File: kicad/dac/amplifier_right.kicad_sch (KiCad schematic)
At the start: 29 parts, among them Q2 PNP, Q3 PNP, Q4 NPN, Q5 NPN, Q6 NPN, Q7 PNP, Q8 NPN, Q9 PNP

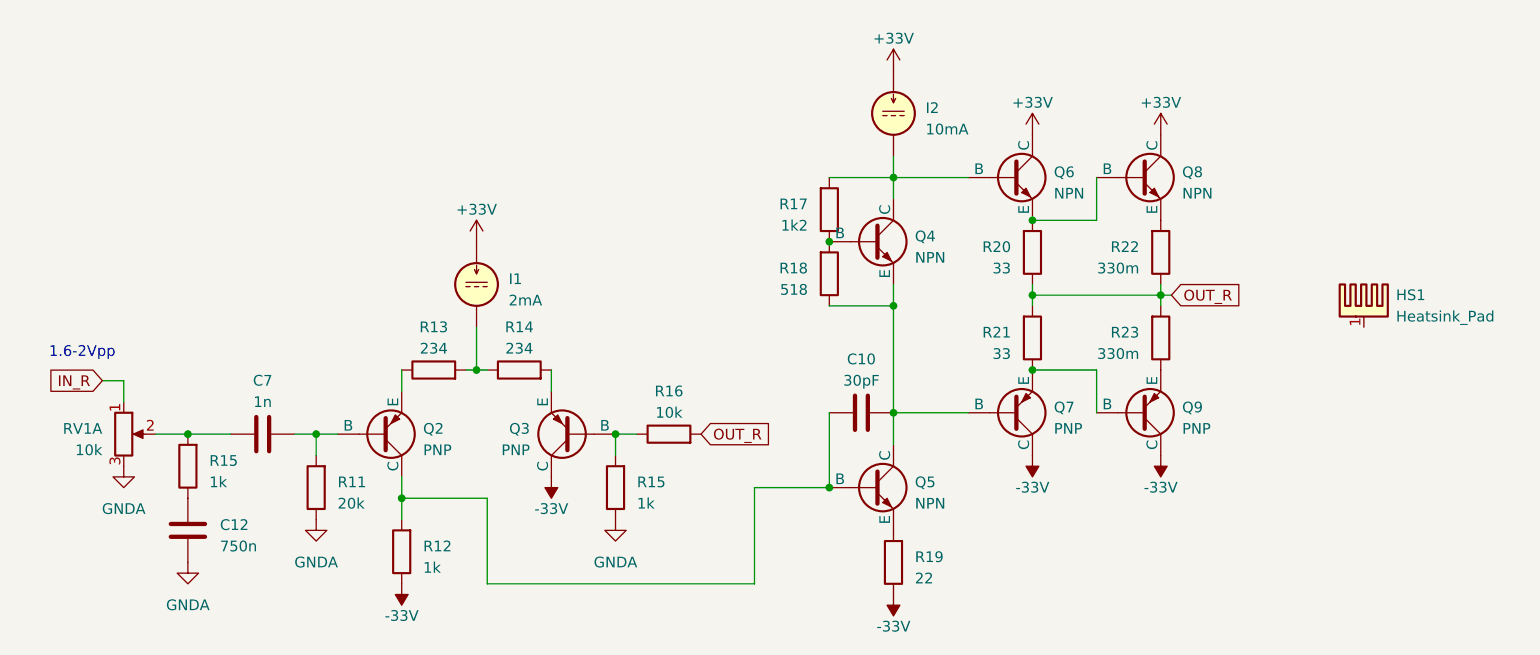
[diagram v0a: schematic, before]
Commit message: split power supply to different board
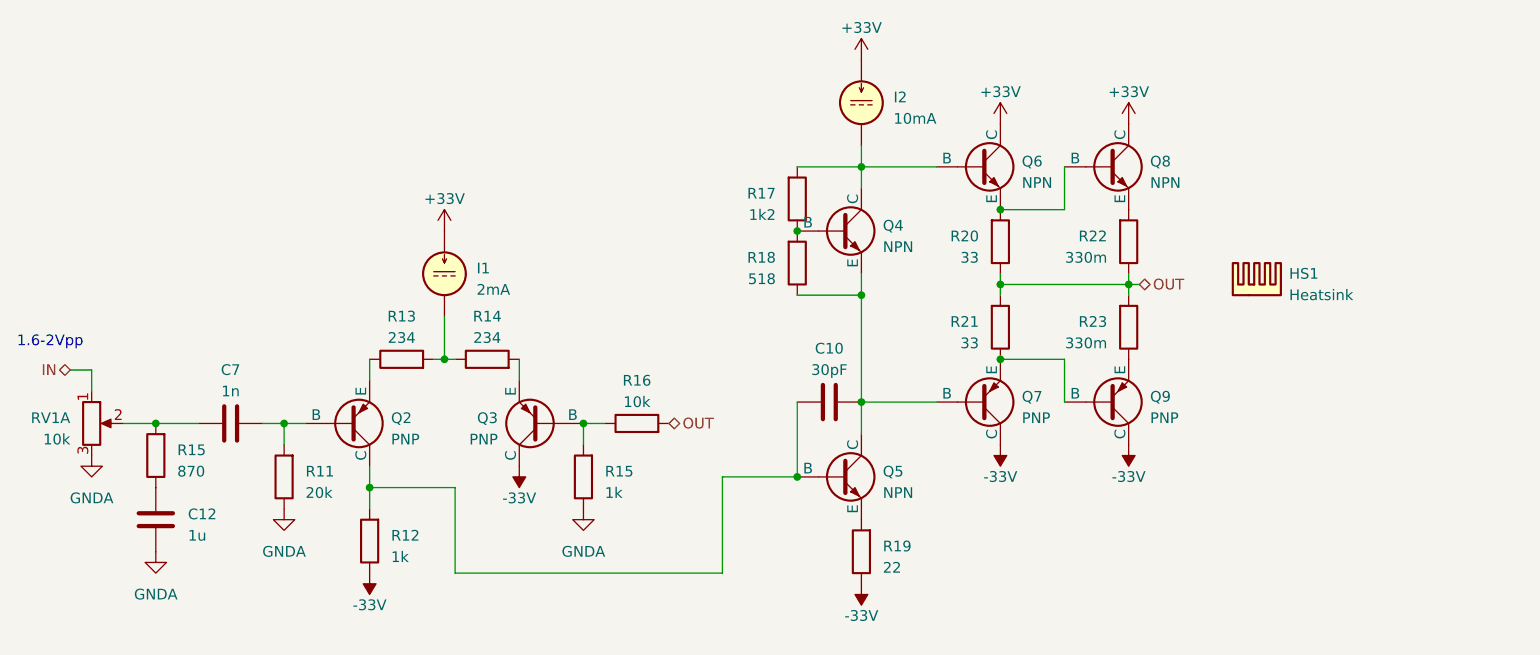
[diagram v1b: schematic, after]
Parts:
- removed HS1: Heatsink_Pad, symbol Mechanical:Heatsink_Pad
- removed R15 (x2): 1k, Resistor_THT:R_Axial_DIN0207_L6.3mm_D2.5mm_P10.16mm_Horizontal, symbol Device:R
- added HS1: Heatsink, Heatsink:Heatsink_Fischer_SK104-STCB_35x13mm__2xDrill3.5mm_ScrewM3, symbol Mechanical:Heatsink
- added R15: 1k, Resistor_THT:R_Axial_DIN0207_L6.3mm_D2.5mm_P10.16mm_Horizontal, symbol Device:R
- added R15: 870, Resistor_THT:R_Axial_DIN0207_L6.3mm_D2.5mm_P10.16mm_Horizontal, symbol Device:R
- C12: value 750n -> 1u
- Q4: footprint (none) -> Package_TO_SOT_THT:TO-92L_Inline
- Q8, Q9: footprint (none) -> Package_TO_SOT_THT:TO-220-3_Vertical
- RV1: footprint (none) -> library:RK09L12B
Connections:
- net GNDA: now also R15.1
- net at Q3.2 (B), R16.1: now also R15.2
- net at C7.1, RV1.2: now also R15.2
- net at C12.1: now also R15.1
- net IN_R renamed IN
- net OUT_R renamed OUT

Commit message: Commit
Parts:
- removed C12: 1u, symbol Device:C
- removed I1: 2mA, symbol Simulation_SPICE:IDC
- removed I2: 10mA, symbol Simulation_SPICE:IDC
- removed Q2, Q3: PNP, symbol Simulation_SPICE:PNP
- removed Q4: NPN, Package_TO_SOT_THT:TO-92L_Inline, symbol Simulation_SPICE:NPN
- removed Q5: NPN, symbol Simulation_SPICE:NPN
- removed R12, R15: 1k, Resistor_THT:R_Axial_DIN0207_L6.3mm_D2.5mm_P10.16mm_Horizontal, symbol Device:R
- removed R13: 234, Resistor_THT:R_Axial_DIN0207_L6.3mm_D2.5mm_P10.16mm_Horizontal, symbol Device:R
- removed R15: 870, Resistor_THT:R_Axial_DIN0207_L6.3mm_D2.5mm_P10.16mm_Horizontal, symbol Device:R
- removed R19: 22, Resistor_THT:R_Axial_DIN0207_L6.3mm_D2.5mm_P10.16mm_Horizontal, symbol Device:R
- removed R20, R21: 33, Resistor_THT:R_Axial_DIN0207_L6.3mm_D2.5mm_P10.16mm_Horizontal, symbol Device:R
- removed R22, R23: 330m, symbol Device:R
- added C11: 120p, symbol Device:C
- added C19: 10u, Capacitor_THT:CP_Radial_D5.0mm_P2.50mm, symbol Device:C_Polarized
- added C20, C21: 10u, symbol Device:C
- added C22, C23: 100u, symbol Device:C_Polarized
- added Q10, Q6: PNP, Package_SO:SC-74-6_1.5x2.9mm_P0.95mm, symbol library:Dual-PNP
- added Q4 (x3): NPN, Package_TO_SOT_THT:TO-92, symbol Simulation_SPICE:NPN
- added unit 2 of Q6
- added unit 2 of Q7
- added Q8: NPN, Package_SO:SC-74-6_1.5x2.9mm_P0.95mm, symbol library:Dual-NPN
- added unit 2 of Q8
- added R12 (x2): 470, Resistor_SMD:R_1206_3216Metric_Pad1.30x1.75mm_HandSolder, symbol Device:R
- added R13: 68, Resistor_THT:R_Axial_DIN0207_L6.3mm_D2.5mm_P10.16mm_Horizontal, symbol Device:R
- added R13: 430, Resistor_SMD:R_1206_3216Metric_Pad1.30x1.75mm_HandSolder, symbol Device:R
- added R13 (x2), R15: 68, Resistor_SMD:R_1206_3216Metric_Pad1.30x1.75mm_HandSolder, symbol Device:R
- added R15 (x2): 27k, Resistor_SMD:R_1206_3216Metric_Pad1.30x1.75mm_HandSolder, symbol Device:R
- added R15: 2k, Resistor_THT:R_Axial_DIN0207_L6.3mm_D2.5mm_P10.16mm_Horizontal, symbol Device:R
- added R15: 680, Resistor_SMD:R_1206_3216Metric_Pad1.30x1.75mm_HandSolder, symbol Device:R
- added R19: 2k2, Resistor_SMD:R_1206_3216Metric_Pad1.30x1.75mm_HandSolder, symbol Device:R
- added R19: 22, Resistor_SMD:R_1206_3216Metric_Pad1.30x1.75mm_HandSolder, symbol Device:R
- added R20 (x2): 33, Resistor_SMD:R_1206_3216Metric_Pad1.30x1.75mm_HandSolder, symbol Device:R
- added R35: 500, symbol Device:R_Trim
- added R37: 100, Resistor_SMD:R_1206_3216Metric_Pad1.30x1.75mm_HandSolder, symbol Device:R
- added R9 (x2): 1, Resistor_THT:R_Axial_DIN0614_L14.3mm_D5.7mm_P20.32mm_Horizontal, symbol Device:R
- added RV2: 100, symbol Device:R_Potentiometer_Trim
- C10: footprint (none) -> Capacitor_SMD:C_1206_3216Metric_Pad1.33x1.80mm_HandSolder
- C7: value 1n -> 2u2
- HS1: footprint Heatsink:Heatsink_Fischer_SK104-STCB_35x13mm__2xDrill3.5mm_ScrewM3 -> Heatsink:Heatsink_Fischer_SK129-STS_42x25mm_2xDrill2.5mm; Digikey (none) -> HS404-ND; DigikeyAlt (none) -> FA-T220-25E-ND; Height (none) -> 25.4mm
- R14: value 234 -> 430; footprint Resistor_THT:R_Axial_DIN0207_L6.3mm_D2.5mm_P10.16mm_Horizontal -> Resistor_SMD:R_1206_3216Metric_Pad1.30x1.75mm_HandSolder
- R16: value 10k -> 20k
- R17: value 1k2 -> 2k2; footprint Resistor_THT:R_Axial_DIN0207_L6.3mm_D2.5mm_P10.16mm_Horizontal -> Resistor_SMD:R_1206_3216Metric_Pad1.30x1.75mm_HandSolder
- R18: value 518 -> 680; footprint Resistor_THT:R_Axial_DIN0207_L6.3mm_D2.5mm_P10.16mm_Horizontal -> Resistor_SMD:R_1206_3216Metric_Pad1.30x1.75mm_HandSolder
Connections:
- net GNDA: now also C11.2, C20.2, C21.1, C22.2, C23.1, Q4.1 (C), R15.1, R15.1, R15.1
- net IN: now also R13.1; no longer RV1.1
- net OUT: now also R20.1, R20.2, R9.1, R9.2
- net at R16.1: now also Q6.2 (B), R15.2
- net at R14.1: now also R13.1, RV2.3
- net at R14.2: now also Q6.4 (E)
- net at C10.2, Q7.2 (B): now also C19.2, Q4.1 (C), Q4.3 (E), R35.2; no longer R18.1
- net at Q7.3 (E), Q9.2 (B): now also R20.1
- net at Q6.2 (B): now also C19.1, Q4.1 (C), R37.2; no longer R17.2
- net at R17.1, R18.2: now also Q4.2 (B)
- net at Q8.3 (E): now also R9.1
- net at Q9.3 (E): now also R9.2
- net at Q6.3 (E), Q8.2 (B): now also R20.2
- net at C7.2, R11.2: now also Q6.1 (B)
- net at C10.1: now also Q4.2 (B), Q6.6 (C), Q8.6 (C)
- net +36V renamed +30V
- net +30V: now also C20.1, C22.1, Q10.5 (E), Q7.5 (E), R15.2, R15.2
- net -36V renamed -30V
- net -30V: now also C21.2, C23.2, R12.1, R12.1, R19.1, R19.1
- new net: Q8.5 (E), R12.2
- new net: Q6.5 (E), R13.1
- new net: C11.1, R13.2, RV1.1
- new net: Q8.4 (E), R12.2
- new net: R13.1, R13.2, RV2.1
- new net: R18.1, R35.1
- new net: Q4.2 (B), Q4.3 (E), R19.2
- new net: Q7.2 (B), Q7.6 (C), R15.2
- new net: Q7.3 (C), R13.2, R13.2, RV2.2
- new net: Q7.1 (B), Q7.4 (E), R15.1
- new net: Q4.3 (E), R19.2
- new net: Q10.1 (B), Q10.4 (E), R15.1
- new net: Q6.3 (C), Q8.1 (B), Q8.2 (B), Q8.3 (C)
- new net: Q10.3 (C), R17.2, R37.1
- new net: Q10.2 (B), Q10.6 (C), R15.2
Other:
- note added: "0.5mA"
- note added: "1.7V above V-"
- note added: "10mA"
- note added: "1mA"
- note added: "=Vbe factor * re'"
- note added: "COPY"
- note added: "Iq=26mA"
- note added: "This sheet for the right channel amplifier is a copy from the left channel. Its design must NOT be changed. Beware of potentiometer A/B variants. All resistors are 1/4W 1206 unless specified."
- note added: "Vbias=4*Vbe"
- title: USB DAC & Headphone Amplifier -> Right Channel Amplifier
- moved on the sheet: RV1A

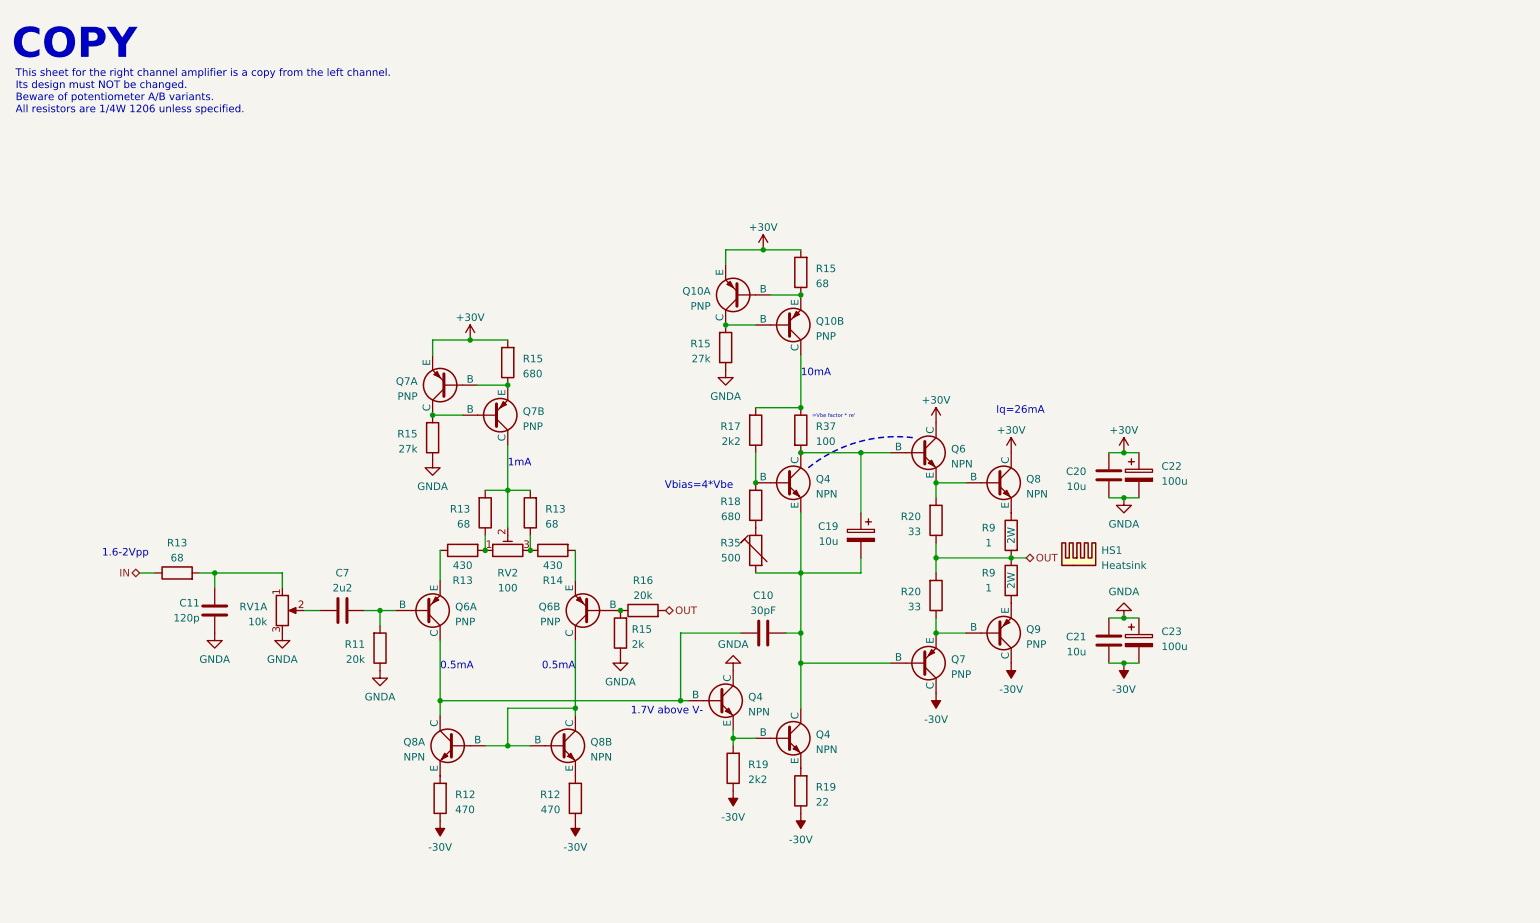
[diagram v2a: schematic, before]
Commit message: completed power supply footprints and placement
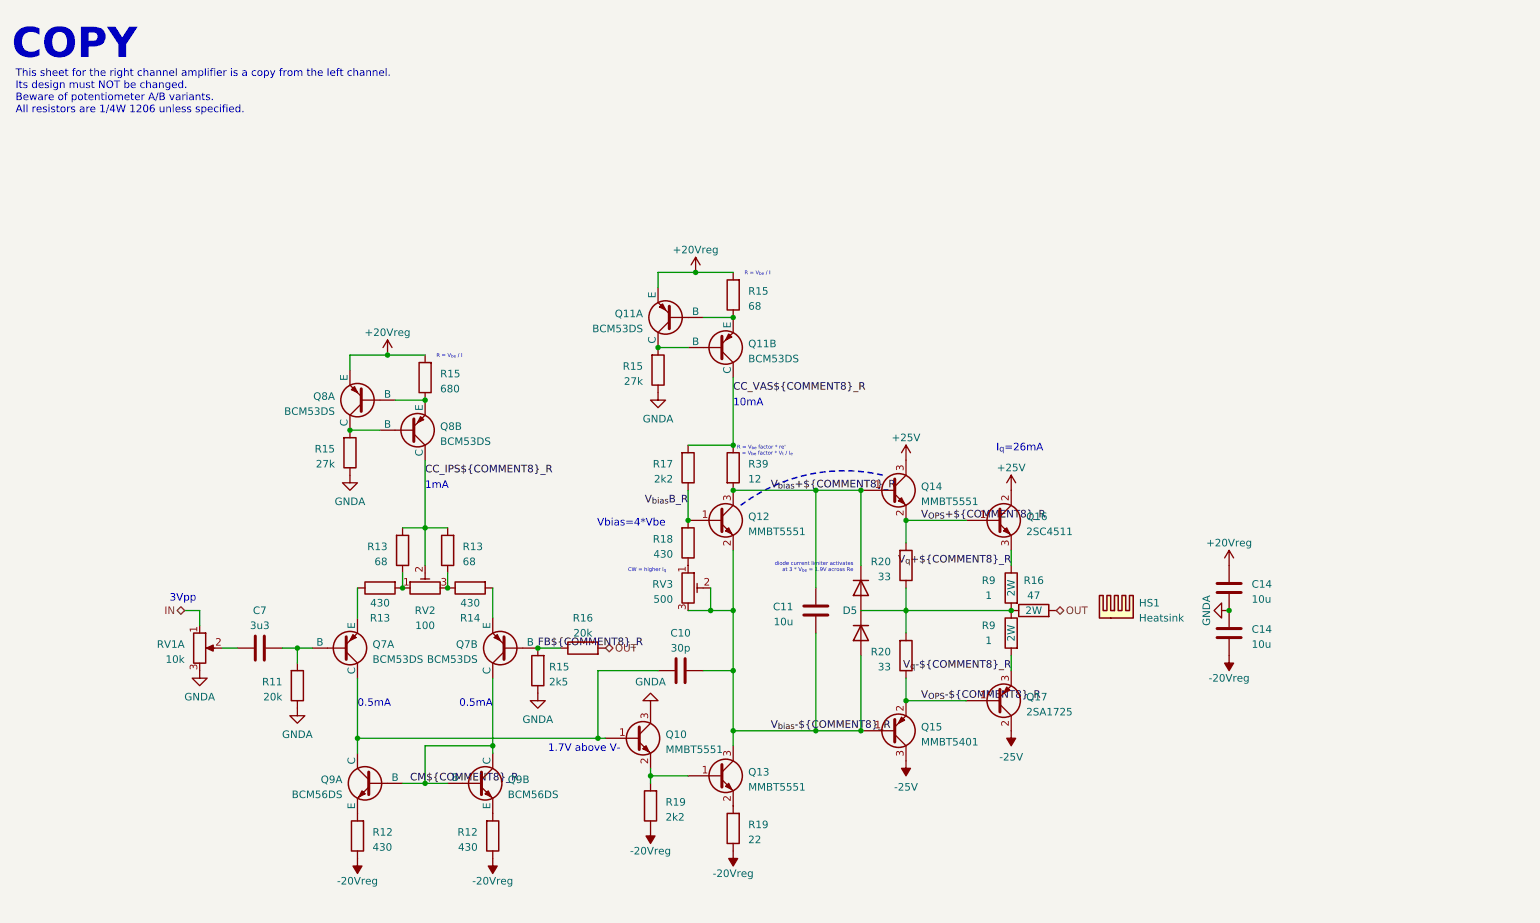
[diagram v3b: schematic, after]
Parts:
- removed C19: 10u, Capacitor_THT:CP_Radial_D5.0mm_P2.50mm, symbol Device:C_Polarized
- removed C20, C21: 10u, symbol Device:C
- removed C22, C23: 100u, symbol Device:C_Polarized
- removed Q10, Q6: PNP, Package_SO:SC-74-6_1.5x2.9mm_P0.95mm, symbol library:Dual-PNP
- removed Q4 (x3): NPN, Package_TO_SOT_THT:TO-92, symbol Simulation_SPICE:NPN
- removed Q6: NPN, symbol Simulation_SPICE:NPN
- removed Q7: PNP, symbol Simulation_SPICE:PNP
- removed Q8: NPN, Package_SO:SC-74-6_1.5x2.9mm_P0.95mm, symbol library:Dual-NPN
- removed Q8: NPN, Package_TO_SOT_THT:TO-220-3_Vertical, symbol Simulation_SPICE:NPN
- removed Q9: PNP, Package_TO_SOT_THT:TO-220-3_Vertical, symbol Simulation_SPICE:PNP
- removed R12 (x2): 470, Resistor_SMD:R_1206_3216Metric_Pad1.30x1.75mm_HandSolder, symbol Device:R
- removed R13: 68, Resistor_THT:R_Axial_DIN0207_L6.3mm_D2.5mm_P10.16mm_Horizontal, symbol Device:R
- removed R13: 430, Resistor_SMD:R_1206_3216Metric_Pad1.30x1.75mm_HandSolder, symbol Device:R
- removed R13 (x2), R15: 68, Resistor_SMD:R_1206_3216Metric_Pad1.30x1.75mm_HandSolder, symbol Device:R
- removed R15 (x2): 27k, Resistor_SMD:R_1206_3216Metric_Pad1.30x1.75mm_HandSolder, symbol Device:R
- removed R15: 2k, Resistor_THT:R_Axial_DIN0207_L6.3mm_D2.5mm_P10.16mm_Horizontal, symbol Device:R
- removed R15: 680, Resistor_SMD:R_1206_3216Metric_Pad1.30x1.75mm_HandSolder, symbol Device:R
- removed R16: 20k, Resistor_THT:R_Axial_DIN0207_L6.3mm_D2.5mm_P10.16mm_Horizontal, symbol Device:R
- removed R19: 2k2, Resistor_SMD:R_1206_3216Metric_Pad1.30x1.75mm_HandSolder, symbol Device:R
- removed R19: 22, Resistor_SMD:R_1206_3216Metric_Pad1.30x1.75mm_HandSolder, symbol Device:R
- removed R20 (x2): 33, Resistor_SMD:R_1206_3216Metric_Pad1.30x1.75mm_HandSolder, symbol Device:R
- removed R35: 500, symbol Device:R_Trim
- removed R37: 100, Resistor_SMD:R_1206_3216Metric_Pad1.30x1.75mm_HandSolder, symbol Device:R
- removed R9 (x2): 1, Resistor_THT:R_Axial_DIN0614_L14.3mm_D5.7mm_P20.32mm_Horizontal, symbol Device:R
- added C14 (x2): 10u, Capacitor_SMD:C_1206_3216Metric_Pad1.33x1.80mm_HandSolder, symbol Device:C
- added D5: ~, Package_TO_SOT_SMD:SOT-23-3, symbol library:Dual_Diode_Array
- added Q10, Q12, Q13, Q14: MMBT5551, Package_TO_SOT_SMD:SOT-23-3, symbol Device:Q_NPN_BEC
- added Q11, Q8: BCM53DS, Package_SO:SC-74-6_1.5x2.9mm_P0.95mm, symbol library:Dual-PNP
- added Q15: MMBT5401, Package_TO_SOT_SMD:SOT-23-3, symbol Device:Q_PNP_BEC
- added Q16: 2SC4511, Package_TO_SOT_THT:TO-220F-3_Vertical, symbol Device:Q_NPN_BCE
- added Q17: 2SA1725, Package_TO_SOT_THT:TO-220F-3_Vertical, symbol Device:Q_PNP_BCE
- added Q9: BCM56DS, Package_SO:SC-74-6_1.5x2.9mm_P0.95mm, symbol library:Dual-NPN
- added R12 (x2), R13: 430, Resistor_SMD:R_1206_3216Metric_Pad1.30x1.75mm_HandSolder, symbol Device:R
- added R13 (x2), R15: 68, Resistor_SMD:R_1206_3216Metric_Pad1.30x1.75mm_HandSolder, symbol Device:R
- added R15: 680, Resistor_SMD:R_1206_3216Metric_Pad1.30x1.75mm_HandSolder, symbol Device:R
- added R15 (x2): 27k, Resistor_SMD:R_1206_3216Metric_Pad1.30x1.75mm_HandSolder, symbol Device:R
- added R15: 2k5, Resistor_THT:R_Axial_DIN0207_L6.3mm_D2.5mm_P10.16mm_Horizontal, symbol Device:R
- added R16: 20k, Resistor_THT:R_Axial_DIN0207_L6.3mm_D2.5mm_P10.16mm_Horizontal, symbol Device:R
- added R16: 47, symbol Device:R
- added R19: 22, Resistor_SMD:R_1206_3216Metric_Pad1.30x1.75mm_HandSolder, symbol Device:R
- added R19: 2k2, Resistor_SMD:R_1206_3216Metric_Pad1.30x1.75mm_HandSolder, symbol Device:R
- added R20 (x2): 33, Resistor_SMD:R_1206_3216Metric_Pad1.30x1.75mm_HandSolder, symbol Device:R
- added R39: 12, Resistor_SMD:R_1206_3216Metric_Pad1.30x1.75mm_HandSolder, symbol Device:R
- added R9 (x2): 1, Resistor_THT:R_Axial_DIN0614_L14.3mm_D5.7mm_P20.32mm_Horizontal, symbol Device:R
- added RV3: 500, library:TC33, symbol Device:R_Potentiometer_Trim
- C10: value 30pF -> 30p
- C11: value 120p -> 10u; footprint (none) -> Capacitor_SMD:C_1206_3216Metric_Pad1.33x1.80mm_HandSolder; Digikey (none) -> 1276-3100-1-ND
- C7: value 2u2 -> 3u3; footprint (none) -> Capacitor_THT:C_Rect_L7.2mm_W7.2mm_P5.00mm_FKS2_FKP2_MKS2_MKP2; Digikey (none) -> 1928-1645-ND; Height (none) -> 13mm
- Q7: value PNP -> BCM53DS; footprint Package_SO:TSOP-6_1.65x3.05mm_P0.95mm -> Package_SO:SC-74-6_1.5x2.9mm_P0.95mm
- R18: value 680 -> 430
- RV2: footprint (none) -> library:TC33; Digikey (none) -> 118-TC33X-2-101GCT-ND
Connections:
- net GNDA: now also C14.1, C14.2, Q10.3 (C), R15.1, R15.1, R15.1; no longer C11.2
- net IN: now also RV1.1
- net OUT: now also R16.2, R16.2
- net at C7.2, R11.2: now also Q7.1 (B)
- net at C10.1: now also Q7.6 (C), Q10.1 (B), Q9.6 (C)
- net V_{bias}+${COMMENT8}${COMMENT9}: now reaches C11.1
- net V_{bias}+${COMMENT8}${COMMENT9}: now also D5.2 (C), Q12.3 (C), Q14.1 (B), R39.2; no longer RV1.1
- net V_{bias}-${COMMENT8}${COMMENT9}: now reaches C10.2
- net V_{bias}-${COMMENT8}${COMMENT9}: now also C11.2, D5.1 (A), Q12.2 (E), Q13.3 (C), Q15.1 (B), RV3.2, RV3.3
- net at RV2.1: now also R13.1, R13.2
- net at R18.1: now also RV3.1
- net FB${COMMENT8}${COMMENT9}: now reaches Q7.2 (B)
- net FB${COMMENT8}${COMMENT9}: now also R15.2, R16.1; no longer Q7.6 (C)
- net CC_IPS${COMMENT8}${COMMENT9}: now reaches RV2.2
- net CC_IPS${COMMENT8}${COMMENT9}: now also Q8.3 (C), R13.2, R13.2; no longer Q7.3 (C)
- net at Q7.4 (E): now also R14.2; no longer Q7.1 (B)
- net at R14.1, RV2.3: now also R13.1
- net CC_VAS${COMMENT8}${COMMENT9}: now reaches R17.2
- net CC_VAS${COMMENT8}${COMMENT9}: now also Q11.3 (C), R39.1
- net V_{bias}B${COMMENT9}: now reaches R17.1, R18.2
- net V_{bias}B${COMMENT9}: now also Q12.1 (B)
- net +30V: no longer names the net of Q7.5 (E)
- net +30V: now also R13.1
- new net: Q11.2 (B), Q11.6 (C), R15.2
- new net: Q11.1 (B), Q11.4 (E), R15.1
- new net: Q9.5 (E), R12.2
- new net: Q8.1 (B), Q8.4 (E), R15.1
- new net: Q8.2 (B), Q8.6 (C), R15.2
- new net: D5.3 (C/A), R16.1, R20.1, R20.2, R9.1, R9.2
- new net: Q10.2 (E), Q13.1 (B), R19.2
- new net: Q13.2 (E), R19.2
- new net: Q9.4 (E), R12.2
- new net +20Vreg: C14.1, Q11.5 (E), Q8.5 (E), R15.2, R15.2
- new net +25V: Q14.3 (C), Q16.2 (C)
- new net -20Vreg: C14.2, R12.1, R12.1, R19.1, R19.1
- new net -25V: Q15.3 (C), Q17.2 (C)
- new net CM${COMMENT8}${COMMENT9}: Q7.3 (C), Q9.1 (B), Q9.2 (B), Q9.3 (C)
- new net V_{OPS}+${COMMENT8}${COMMENT9}: Q14.2 (E), Q16.1 (B), R20.2
- new net V_{OPS}-${COMMENT8}${COMMENT9}: Q15.2 (E), Q17.1 (B), R20.1
- new net V_{q}+${COMMENT8}${COMMENT9}: Q16.3 (E), R9.1
- new net V_{q}-${COMMENT8}${COMMENT9}: Q17.3 (E), R9.2
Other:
- note added: "3Vpp"
- note added: "CW = higher I_{q}"
- note added: "I_{q}=26mA"
- note added: "R = V_{be} / I"
- note added: "R = V_{be} factor * re' = V_{be} factor * V_{t} / I_{e}"
- note added: "diode current limiter activates at 3 * V_{be} = 1.9V across Re"
- note removed: "1.6-2Vpp"
- note removed: "=Vbe factor * re'"
- note removed: "Iq=26mA"
- company: (none) -> Author: Jona Heinke
- moved on the sheet: RV1A
